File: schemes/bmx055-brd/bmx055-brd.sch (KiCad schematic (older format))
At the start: 17 parts, among them P1 vcc, P2 gnd, P3 accel-cs, P4 gyro-cs, P5 magnet-cs, P6 sck, P7 mosi, P8 miso, U1 BMX055

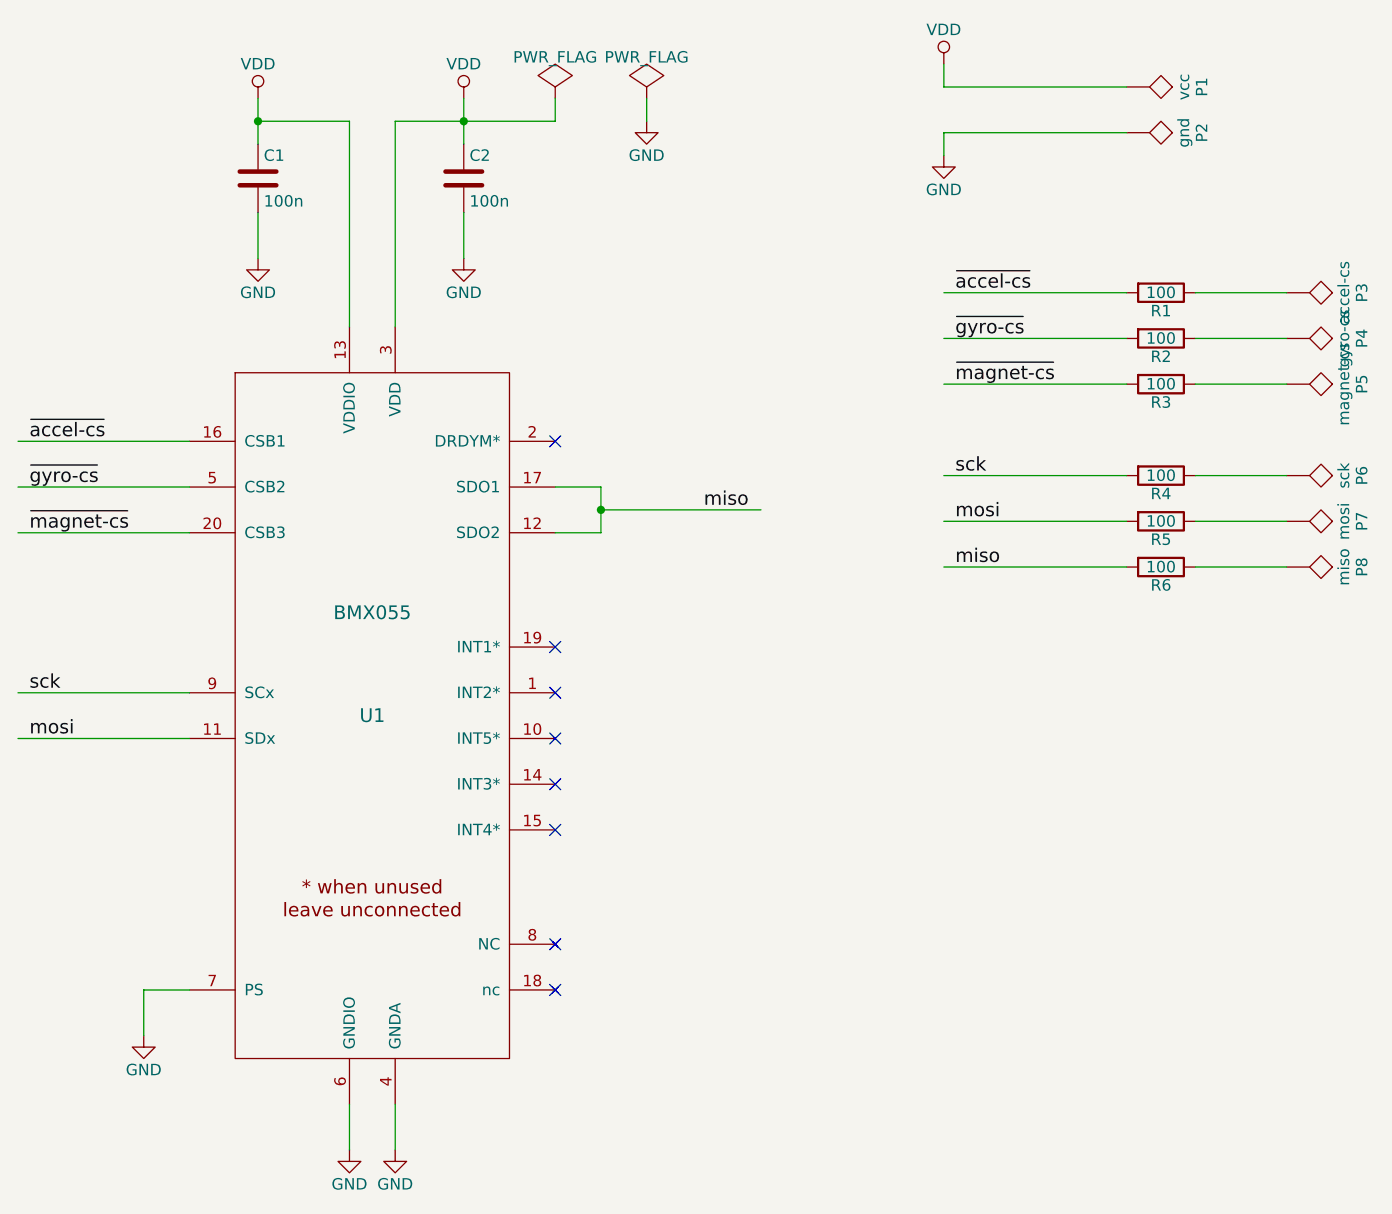
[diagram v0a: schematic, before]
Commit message: Remade board for I2C mode and prepared for tonner transfer.
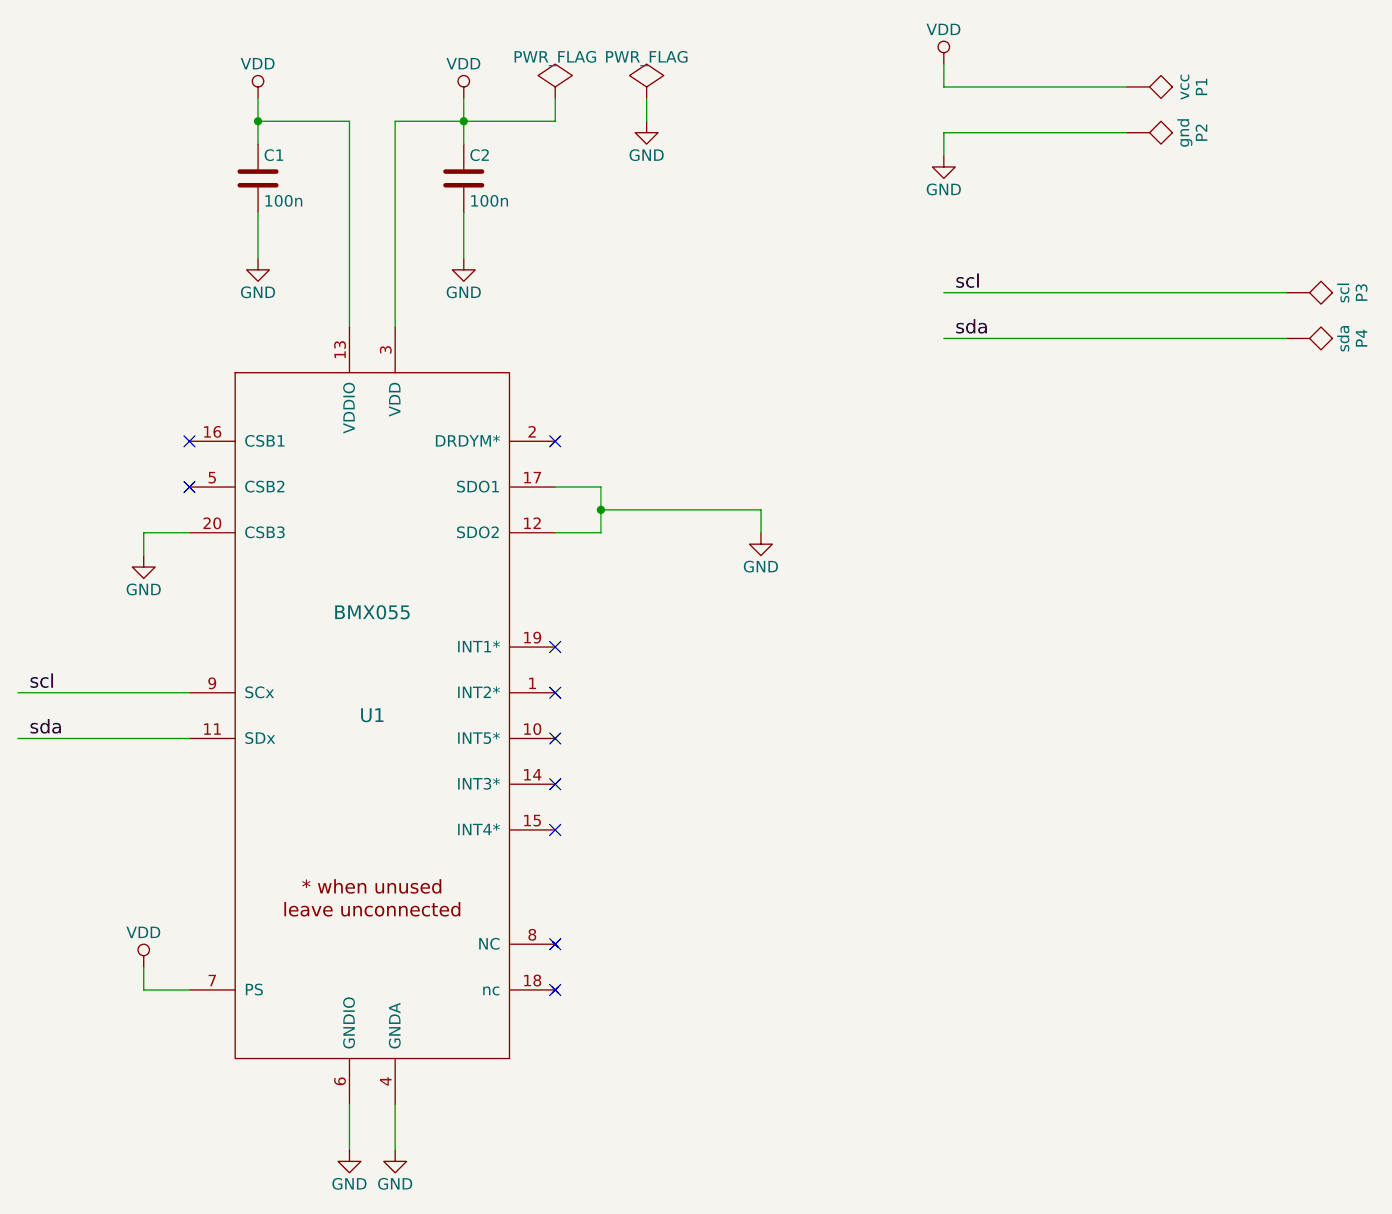
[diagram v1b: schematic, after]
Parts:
- removed P5: magnet-cs, symbol TST
- removed P6: sck, symbol TST
- removed P7: mosi, symbol TST
- removed P8: miso, symbol TST
- removed R1, R2, R3, R4, R5, R6: 100, symbol R
- C1, C2: footprint (none) -> Capacitors_SMD:C_0805
- P1, P2: footprint (none) -> Measurement_Points:Measurement_Point_Round-SMD-Pad_Small
- P3: value accel-cs -> scl; footprint (none) -> Measurement_Points:Measurement_Point_Round-SMD-Pad_Small
- P4: value gyro-cs -> sda; footprint (none) -> Measurement_Points:Measurement_Point_Round-SMD-Pad_Small
- U1: footprint (none) -> libs:bmx055-w
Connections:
- net labels added: scl, sda
- net labels removed: miso, mosi, sck, ~accel-cs~, ~gyro-cs~, ~magnet-cs~
- wire segments 39 -> 29
- no-connect marks 8 -> 10
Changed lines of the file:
@@
 LIBS:valves
 LIBS:bmx055
+LIBS:bmx055-brd-cache
 EELAYER 25 0
 EELAYER END
@@
 F 0 "U1" H 4500 4250 60  0000 C CNN
 F 1 "BMX055" H 4500 4700 60  0000 C CNN
-F 2 "" H 4500 3550 60  0001 C CNN
+F 2 "libs:bmx055-w" H 4500 3550 60  0001 C CNN
 F 3 "" H 4500 3550 60  0001 C CNN
 	1    4500 4250
@@
 F 0 "C1" H 4025 2000 50  0000 L CNN
 F 1 "100n" H 4025 1800 50  0000 L CNN
-F 2 "" H 4038 1750 50  0000 C CNN
+F 2 "Capacitors_SMD:C_0805" H 4038 1750 50  0001 C CNN
 F 3 "" H 4000 1900 50  0000 C CNN
 	1    4000 1900
@@
 F 0 "C2" H 4925 2000 50  0000 L CNN
 F 1 "100n" H 4925 1800 50  0000 L CNN
-F 2 "" H 4938 1750 50  0000 C CNN
+F 2 "Capacitors_SMD:C_0805" H 4938 1750 50  0001 C CNN
 F 3 "" H 4900 1900 50  0000 C CNN
 	1    4900 1900
@@
 Wire Wire Line
 	3700 4350 2950 4350
+Text Label 3000 4150 0    60   ~ 0
+scl
+Wire Wire Line
+	3700 4150 2950 4150
 Text Label 3000 4350 0    60   ~ 0
-mosi
-Wire Wire Line
-	3700 4150 2950 4150
-Text Label 3000 4150 0    60   ~ 0
-sck
+sda
 Wire Wire Line
 	5300 3250 5500 3250
@@
 	5500 3350 6200 3350
 Connection ~ 5500 3350
-Text Label 5950 3350 0    60   ~ 0
-miso
-Wire Wire Line
-	3700 3050 2950 3050
-Text Label 3000 3050 0    60   ~ 0
-~accel-cs~
-Wire Wire Line
-	3700 3250 2950 3250
-Text Label 3000 3250 0    60   ~ 0
-~gyro-cs~
-Wire Wire Line
-	3700 3450 2950 3450
-Text Label 3000 3450 0    60   ~ 0
-~magnet-cs~
 NoConn ~ 5300 3950
 NoConn ~ 5300 4150
@@
 Wire Wire Line
 	3700 5450 3500 5450
-Wire Wire Line
-	3500 5450 3500 5650
-$Comp
-L GND #PWR07
-U 1 1 57D71D3F
-P 3500 5650
-F 0 "#PWR07" H 3500 5400 50  0001 C CNN
-F 1 "GND" H 3500 5500 50  0000 C CNN
-F 2 "" H 3500 5650 50  0000 C CNN
-F 3 "" H 3500 5650 50  0000 C CNN
-	1    3500 5650
-	1    0    0    -1
-$EndComp
 NoConn ~ 5300 3050
 Wire Wire Line
-	7000 3400 7800 3400
-Text Label 7050 3400 0    60   ~ 0
-mosi
-Wire Wire Line
-	7000 3200 7800 3200
-Text Label 7050 3200 0    60   ~ 0
-sck
-Wire Wire Line
-	7000 2400 7800 2400
+	7000 2400 8500 2400
 Text Label 7050 2400 0    60   ~ 0
-~accel-cs~
-Wire Wire Line
-	7000 2600 7800 2600
+scl
+Wire Wire Line
+	7000 2600 8500 2600
 Text Label 7050 2600 0    60   ~ 0
-~gyro-cs~
-Wire Wire Line
-	7000 2800 7800 2800
-Text Label 7050 2800 0    60   ~ 0
-~magnet-cs~
-Wire Wire Line
-	7000 3600 7800 3600
-Text Label 7050 3600 0    60   ~ 0
-miso
-$Comp
-L VDD #PWR08
+sda
+$Comp
+L VDD #PWR07
 U 1 1 57D7204F
 P 7000 1400
-F 0 "#PWR08" H 7000 1250 50  0001 C CNN
+F 0 "#PWR07" H 7000 1250 50  0001 C CNN
 F 1 "VDD" H 7000 1550 50  0000 C CNN
 F 2 "" H 7000 1400 50  0000 C CNN
@@
 	7000 1500 7800 1500
 $Comp
-L GND #PWR09
+L GND #PWR08
 U 1 1 57D72087
 P 7000 1800
-F 0 "#PWR09" H 7000 1550 50  0001 C CNN
+F 0 "#PWR08" H 7000 1550 50  0001 C CNN
 F 1 "GND" H 7000 1650 50  0000 C CNN
 F 2 "" H 7000 1800 50  0000 C CNN
@@
 	7000 1700 7800 1700
 $Comp
-L R R1
-U 1 1 57D722A1
-P 7950 2400
-F 0 "R1" V 8030 2400 50  0000 C CNN
-F 1 "100" V 7950 2400 50  0000 C CNN
-F 2 "" V 7880 2400 50  0000 C CNN
-F 3 "" H 7950 2400 50  0000 C CNN
-	1    7950 2400
-	0    1    1    0
-$EndComp
-Wire Wire Line
-	8100 2400 8500 2400
-$Comp
 L TST P3
 U 1 1 57D723A1
 P 8500 2400
 F 0 "P3" H 8500 2700 50  0000 C BNN
-F 1 "accel-cs" H 8500 2650 50  0000 C CNN
-F 2 "" H 8500 2400 50  0000 C CNN
+F 1 "scl" H 8500 2650 50  0000 C CNN
+F 2 "Measurement_Points:Measurement_Point_Round-SMD-Pad_Small" H 8500 2400 50  0001 C CNN
 F 3 "" H 8500 2400 50  0000 C CNN
 	1    8500 2400
 	0    1    1    0
 $EndComp
-$Comp
-L R R2
-U 1 1 57D72417
-P 7950 2600
-F 0 "R2" V 8030 2600 50  0000 C CNN
-F 1 "100" V 7950 2600 50  0000 C CNN
-F 2 "" V 7880 2600 50  0000 C CNN
-F 3 "" H 7950 2600 50  0000 C CNN
-	1    7950 2600
-	0    1    1    0
-$EndComp
-Wire Wire Line
-	8100 2600 8500 2600
 $Comp
 L TST P4
@@
 P 8500 2600
 F 0 "P4" H 8500 2900 50  0000 C BNN
-F 1 "gyro-cs" H 8500 2850 50  0000 C CNN
-F 2 "" H 8500 2600 50  0000 C CNN
+F 1 "sda" H 8500 2850 50  0000 C CNN
+F 2 "Measurement_Points:Measurement_Point_Round-SMD-Pad_Small" H 8500 2600 50  0001 C CNN
 F 3 "" H 8500 2600 50  0000 C CNN
 	1    8500 2600
-	0    1    1    0
-$EndComp
-$Comp
-L R R3
-U 1 1 57D7244C
-P 7950 2800
-F 0 "R3" V 8030 2800 50  0000 C CNN
-F 1 "100" V 7950 2800 50  0000 C CNN
-F 2 "" V 7880 2800 50  0000 C CNN
-F 3 "" H 7950 2800 50  0000 C CNN
-	1    7950 2800
-	0    1    1    0
-$EndComp
-Wire Wire Line
-	8100 2800 8500 2800
-$Comp
-L TST P5
-U 1 1 57D72453
-P 8500 2800
-F 0 "P5" H 8500 3100 50  0000 C BNN
-F 1 "magnet-cs" H 8500 3050 50  0000 C CNN
-F 2 "" H 8500 2800 50  0000 C CNN
-F 3 "" H 8500 2800 50  0000 C CNN
-	1    8500 2800
-	0    1    1    0
-$EndComp
-$Comp
-L R R4
-U 1 1 57D72495
-P 7950 3200
-F 0 "R4" V 8030 3200 50  0000 C CNN
-F 1 "100" V 7950 3200 50  0000 C CNN
-F 2 "" V 7880 3200 50  0000 C CNN
-F 3 "" H 7950 3200 50  0000 C CNN
-	1    7950 3200
-	0    1    1    0
-$EndComp
-Wire Wire Line
-	8100 3200 8500 3200
-$Comp
-L TST P6
-U 1 1 57D7249C
-P 8500 3200
-F 0 "P6" H 8500 3500 50  0000 C BNN
-F 1 "sck" H 8500 3450 50  0000 C CNN
-F 2 "" H 8500 3200 50  0000 C CNN
-F 3 "" H 8500 3200 50  0000 C CNN
-	1    8500 3200
-	0    1    1    0
-$EndComp
-$Comp
-L R R5
-U 1 1 57D724D2
-P 7950 3400
-F 0 "R5" V 8030 3400 50  0000 C CNN
-F 1 "100" V 7950 3400 50  0000 C CNN
-F 2 "" V 7880 3400 50  0000 C CNN
-F 3 "" H 7950 3400 50  0000 C CNN
-	1    7950 3400
-	0    1    1    0
-$EndComp
-Wire Wire Line
-	8100 3400 8500 3400
-$Comp
-L TST P7
-U 1 1 57D724D9
-P 8500 3400
-F 0 "P7" H 8500 3700 50  0000 C BNN
-F 1 "mosi" H 8500 3650 50  0000 C CNN
-F 2 "" H 8500 3400 50  0000 C CNN
-F 3 "" H 8500 3400 50  0000 C CNN
-	1    8500 3400
-	0    1    1    0
-$EndComp
-$Comp
-L R R6
-U 1 1 57D72513
-P 7950 3600
-F 0 "R6" V 8030 3600 50  0000 C CNN
-F 1 "100" V 7950 3600 50  0000 C CNN
-F 2 "" V 7880 3600 50  0000 C CNN
-F 3 "" H 7950 3600 50  0000 C CNN
-	1    7950 3600
-	0    1    1    0
-$EndComp
-Wire Wire Line
-	8100 3600 8500 3600
-$Comp
-L TST P8
-U 1 1 57D7251A
-P 8500 3600
-F 0 "P8" H 8500 3900 50  0000 C BNN
-F 1 "miso" H 8500 3850 50  0000 C CNN
-F 2 "" H 8500 3600 50  0000 C CNN
-F 3 "" H 8500 3600 50  0000 C CNN
-	1    8500 3600
 	0    1    1    0
 $EndComp
@@
 F 0 "P1" H 7800 1800 50  0000 C BNN
 F 1 "vcc" H 7800 1750 50  0000 C CNN
-F 2 "" H 7800 1500 50  0000 C CNN
+F 2 "Measurement_Points:Measurement_Point_Round-SMD-Pad_Small" H 7800 1500 50  0001 C CNN
 F 3 "" H 7800 1500 50  0000 C CNN
 	1    7800 1500
@@
 F 0 "P2" H 7800 2000 50  0000 C BNN
 F 1 "gnd" H 7800 1950 50  0000 C CNN
-F 2 "" H 7800 1700 50  0000 C CNN
+F 2 "Measurement_Points:Measurement_Point_Round-SMD-Pad_Small" H 7800 1700 50  0001 C CNN
 F 3 "" H 7800 1700 50  0000 C CNN
 	1    7800 1700
@@
 $EndComp
 $Comp
-L PWR_FLAG #FLG010
+L PWR_FLAG #FLG09
 U 1 1 57D729F8
 P 5300 1550
-F 0 "#FLG010" H 5300 1645 50  0001 C CNN
+F 0 "#FLG09" H 5300 1645 50  0001 C CNN
 F 1 "PWR_FLAG" H 5300 1730 50  0000 C CNN
 F 2 "" H 5300 1550 50  0000 C CNN
@@
 	5300 1650 5300 1550
 $Comp
-L PWR_FLAG #FLG011
+L PWR_FLAG #FLG010
 U 1 1 57D730EA
 P 5700 1550
-F 0 "#FLG011" H 5700 1645 50  0001 C CNN
+F 0 "#FLG010" H 5700 1645 50  0001 C CNN
 F 1 "PWR_FLAG" H 5700 1730 50  0000 C CNN
 F 2 "" H 5700 1550 50  0000 C CNN
@@
 	5700 1550 5700 1650
 $Comp
-L GND #PWR012
+L GND #PWR011
 U 1 1 57D733B7
 P 5700 1650
-F 0 "#PWR012" H 5700 1400 50  0001 C CNN
+F 0 "#PWR011" H 5700 1400 50  0001 C CNN
 F 1 "GND" H 5700 1500 50  0000 C CNN
 F 2 "" H 5700 1650 50  0000 C CNN
@@
 	1    0    0    -1
 $EndComp
+Wire Wire Line
+	3500 3450 3500 3550
+$Comp
+L GND #PWR012
+U 1 1 57D86788
+P 3500 3550
+F 0 "#PWR012" H 3500 3300 50  0001 C CNN
+F 1 "GND" H 3500 3400 50  0000 C CNN
+F 2 "" H 3500 3550 50  0000 C CNN
+F 3 "" H 3500 3550 50  0000 C CNN
+	1    3500 3550
+	1    0    0    -1
+$EndComp
+NoConn ~ 3700 3050
+NoConn ~ 3700 3250
+Wire Wire Line
+	3700 3450 3500 3450
+Wire Wire Line
+	6200 3350 6200 3450
+$Comp
+L GND #PWR013
+U 1 1 57D869DF
+P 6200 3450
+F 0 "#PWR013" H 6200 3200 50  0001 C CNN
+F 1 "GND" H 6200 3300 50  0000 C CNN
+F 2 "" H 6200 3450 50  0000 C CNN
+F 3 "" H 6200 3450 50  0000 C CNN
+	1    6200 3450
+	1    0    0    -1
+$EndComp
+$Comp
+L VDD #PWR014
+U 1 1 57D86BFA
+P 3500 5350
+F 0 "#PWR014" H 3500 5200 50  0001 C CNN
+F 1 "VDD" H 3500 5500 50  0000 C CNN
+F 2 "" H 3500 5350 50  0000 C CNN
+F 3 "" H 3500 5350 50  0000 C CNN
+	1    3500 5350
+	1    0    0    -1
+$EndComp
+Wire Wire Line
+	3500 5450 3500 5350
 $EndSCHEMATC
